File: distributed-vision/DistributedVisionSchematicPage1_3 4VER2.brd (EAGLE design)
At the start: 123 x 98.5 mm, 157 parts, among them J1 USBR-A-D-F-O-TH, J12 ARJM11C7-104-AB-EW2, J2 RASPBERRRY_COMPUTE_CM3, J6 DM3D-SF, J8 1-84952-5, J9 1-84952-5, Q2 BSS127, Q3 BSS127, Q7 25 MHz, U1 LM26420XMH, U11 IFX91041, U12 TPS26600PWPR, U3 LAN9513-JZXQFN64_9X9MC_MCH-M, U8 SP3003-02, U9 SP3003-02, X1 JST-XH-02-PIN-LONG-PAD

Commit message: Version 3
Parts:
- removed D6: GREEN, RoboJackets-LEDs:LED-0603
- removed JP1: (no value), RoboJackets-Connectors:1X02
- removed Q2, Q3: BSS127, RoboJackets-Discrete:SOT-23-3
- removed R1: 47k, rcl:R0603
- removed R4: 100k, rcl:R0603
- removed R44: 470r, rcl:R0603
- moved H1 81.0 mm to (101.9, 86.1)
- moved C18 21.5 mm to (106.0, 32.8)
- moved L7 19.8 mm to (12.4, 15.1), turned to 180 degrees
- moved R8 17.1 mm to (16.1, 22.0)
- moved C86 16.1 mm to (20.2, 33.9)
- moved C81 15.8 mm to (104.8, 18.0)
- moved C35 14.9 mm to (108.1, 37.9)
- moved C80 14.8 mm to (106.9, 20.6)
- moved C82 14.3 mm to (107.8, 30.3)
- moved U9 14.3 mm to (15.9, 18.2)
- moved H2 14.1 mm to (22.3, 86.1)
- moved C6 13.4 mm to (107.7, 24.1)
- moved C24 13.4 mm to (10.2, 26.9)
- moved C62 13.4 mm to (9.97, 38.9)
- moved C78 13.4 mm to (107.8, 27.3)
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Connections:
- removed net AGND: H1.B2,8, H2.B2,8
- removed net EMMC_DISABLE_N: J2.2, Q2.3
- removed net EMMC_EN_N_1V8: J2.90, Q3.1, R4.1
- removed net N$31: Q2.2, Q3.3, R44.1
- removed net N$32: D6.C, R44.2
- removed net N$33: JP1.2, Q2.1, R1.2
- net +1.8V: no longer R4.2
- net +3.3V: no longer D6.A
- net +5V: no longer JP1.1
- net GND: no longer Q3.2, R1.1
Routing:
- net EMMC_EN_N_1V8: track 85.1 -> 0.00 mm, vias 3 -> 0
- net G_LED+: track 6.71 -> 60.6 mm, vias 0 -> 4
- net N$56: track 43.1 -> 93.7 mm
- net GND: track 1089.3 -> 1047.8 mm, vias 66 -> 67
- net +3.3V-A: track 84.0 -> 111.5 mm
- net EMMC_DISABLE_N: track 22.8 -> 0.00 mm
- net TVCC: track 59.1 -> 37.1 mm, vias 3 -> 1
- net USBDP3: track 74.3 -> 52.7 mm, vias 3 -> 2
- net N$33: track 18.8 -> 0.00 mm, vias 2 -> 0
- net N$40: track 75.0 -> 57.4 mm
- net N$25: track 11.7 -> 29.2 mm
- net USBDM2: track 72.9 -> 57.0 mm
- net N$31: track 15.6 -> 0.00 mm, vias 2 -> 0
- net +3.3V: track 579.1 -> 594.3 mm, vias 36 -> 39
- net VBATT: track 37.5 -> 51.7 mm, vias 3 -> 4
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- added copper zone on layer 1, net GND
- added copper zone on layer 16, net GND
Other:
- board size 123 x 98.5 mm -> 104 x 97.5 mm

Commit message: Joe Cleanup Schematic
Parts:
- removed C53: 100n, rcl:C0402
- removed R2: (no value), rcl:R0603
- removed R31: 4.7k, RoboJackets-Resistors:RC0805N
- F2: value 1A (Trip) -> 2A; device ethernet_poe:0ZCG_BEL -> RoboJackets-Fuses:1812
- R26: value 12k -> 12k, 1.0%
- R27: value 12.4k -> 12.4k, 1.0%
- R7: value 5r1 -> 5.1
- moved C75 117.6 mm to (8.00, -14.0)
- moved R14 94.2 mm to (8.00, -37.0)
- moved R7 89.3 mm to (8.00, -42.0), turned to 0 degrees
- moved F2 81.0 mm to (10.0, -49.0), turned to 0 degrees
- moved R13 77.1 mm to (18.0, -32.0), turned to 0 degrees
- moved R9 77.1 mm to (18.0, -37.0)
- moved C25 62.7 mm to (15.0, -24.0), turned to 0 degrees
- moved R8 59.1 mm to (13.0, -37.0), flipped to the top, turned to 0 degrees
- moved C24 59.0 mm to (13.0, -32.0)
- moved F1 58.1 mm to (10.0, -26.0), turned to 0 degrees
- moved C86 54.3 mm to (8.00, -19.0), turned to 0 degrees
- moved C23 52.3 mm to (8.00, -32.0)
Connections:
- removed net BD+: J1.A03, U9.4
- removed net N$61: C53.1, R31.1, U3.12
- removed net USBDM3: U3.3
- removed net USBDP2: U3.2
- removed net USBDP3: J1.B02, J1.B03, U3.4, U8.4, U8.6
- removed net USB_DM: U3.58
- removed net USB_DP: U3.59
- removed net USB_OTGID: J2.168, R2.2
- removed net VBATT: C18.1, C19.1, C21.1, C22.1, C35.1, J2.197, J2.198, J2.199, J2.200
- new net N$12: U8.6
- new net N$3: R13.2, U1.8
- new net N$6: U9.4
- new net N$7: U8.4
- new net RX_P1: R9.2, U1.12
- new net USB0_N: J2.167, U3.58
- new net USB0_P: J2.165, U3.59
- new net USB2_N: J1.A02, U3.1
- new net USB2_P: J1.A03, U3.2
- new net USB3_N: J1.B02, U3.3
- new net USB3_P: J1.B03, U3.4
- net +3.3V: now also U3.12; no longer R31.2
- net +5V: now also C18.1, C19.1, C21.1, C22.1, C35.1, J2.197, J2.198, J2.199, J2.200
- net BVCC: no longer J1.A01
- net GND: now also J1.S1, J1.S2, J1.S3, J1.S4, J2.168; no longer C53.2, R2.1
- net RX_P: no longer R9.2, U1.12
- net TVCC: now also J1.A01
- net USBDM2: no longer J1.A02, U3.1
- net VDD18CORE: no longer R13.2, U1.8
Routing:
- net +5V: track 172.0 -> 89.1 mm, vias 17 -> 9
- net N$40: track 57.4 -> 0.00 mm, vias 3 -> 0
- net USBDP3: track 52.7 -> 0.00 mm, vias 2 -> 0
- net VBATT: track 51.7 -> 0.00 mm, vias 4 -> 0
- net USBDM2: track 57.0 -> 5.68 mm, vias 3 -> 1
- net USB2_N: track 0.00 -> 49.1 mm, vias 0 -> 2
- net GND: track 1047.8 -> 1001.1 mm, vias 67 -> 65
- net N$5: track 39.7 -> 0.00 mm, vias 4 -> 0
- net +3.3V: track 594.3 -> 561.5 mm, vias 39 -> 42
- net USB_OTGID: track 20.0 -> 0.00 mm
- net USB3_P: track 0.00 -> 13.4 mm, vias 0 -> 2
- net TVCC: track 37.1 -> 24.4 mm
- net +5V_PREFUSE: track 54.1 -> 42.6 mm
- net N$61: track 11.3 -> 0.00 mm, vias 3 -> 0
- net BVCC: track 56.5 -> 48.1 mm
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
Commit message: Joe Small board cleanup
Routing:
- net GND: track 1001.1 -> 8.45 mm, vias 65 -> 3
- net +3.3V-A: track 111.5 -> 106.8 mm
- net VDD18CORE: track 113.7 -> 112.6 mm

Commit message: Updated Values in DisbVision sch
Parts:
- C10, C15, C16, C21, C42, C45, C46, C5, C50, C6, C60, C63, C68, C69, C70, C71, C78, C81, C82, C83, C84, C88, C91: value 100n -> 100nF
- C102, C103, C12, C17, C22, C35, C7, C73: value 10u -> 10uF
- C13, C18, C19, C20, C33, C4, C51, C52, C58, C61, C75, C76, C77, C8, C80, C85, C86, C9: value 10n -> 10nF
- C14, C64: value 1u -> 1uF
- C23, C24, C26, C27, C28, C29: value 22u -> 22uF
- C25: value 470n -> 470nF
- C43, C44, C62: value 4u7 -> 4.7uF
- C65, C66: value 33p -> 33pF

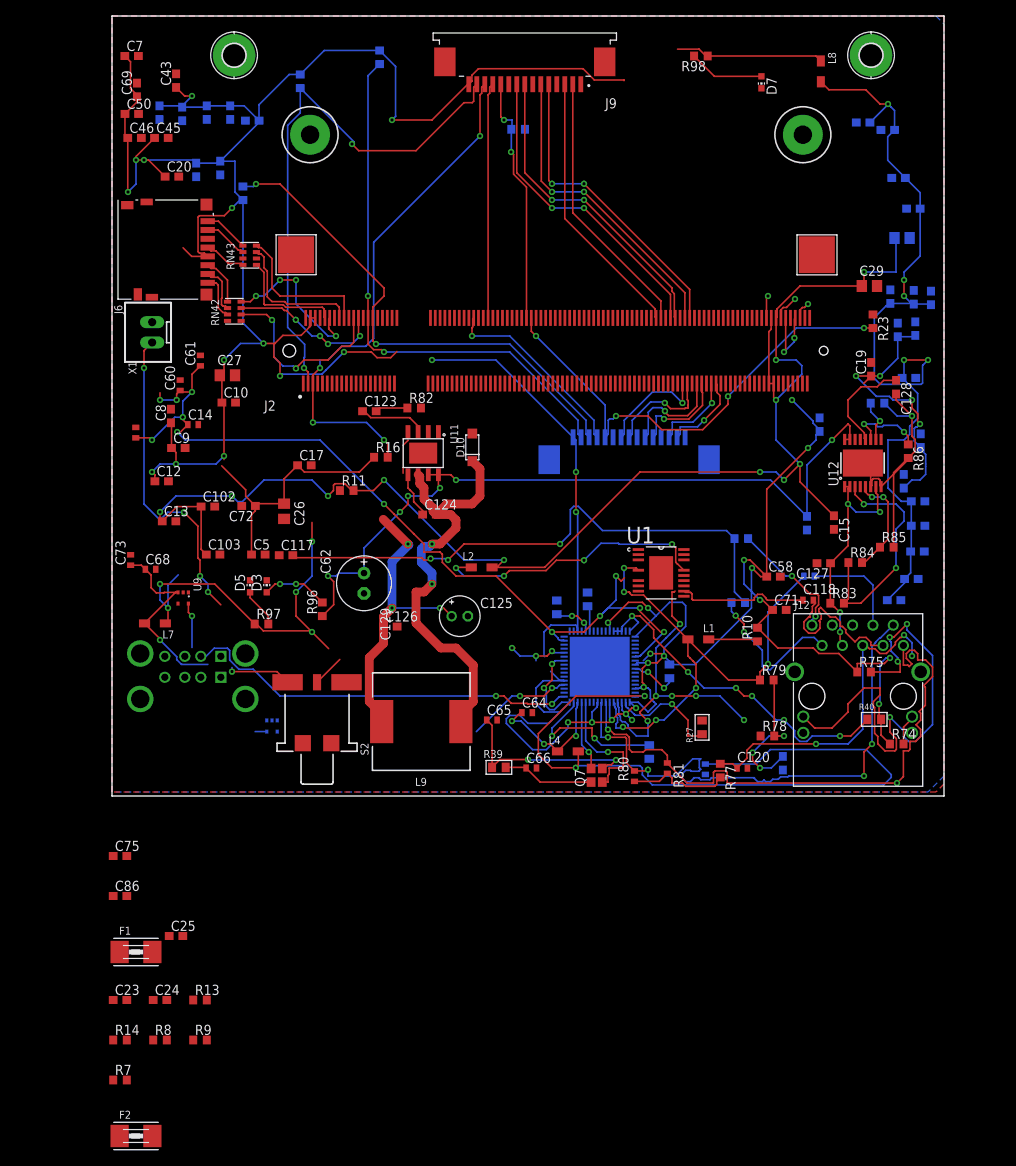
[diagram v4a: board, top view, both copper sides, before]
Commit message: Routed Board Based off Schematic Changes
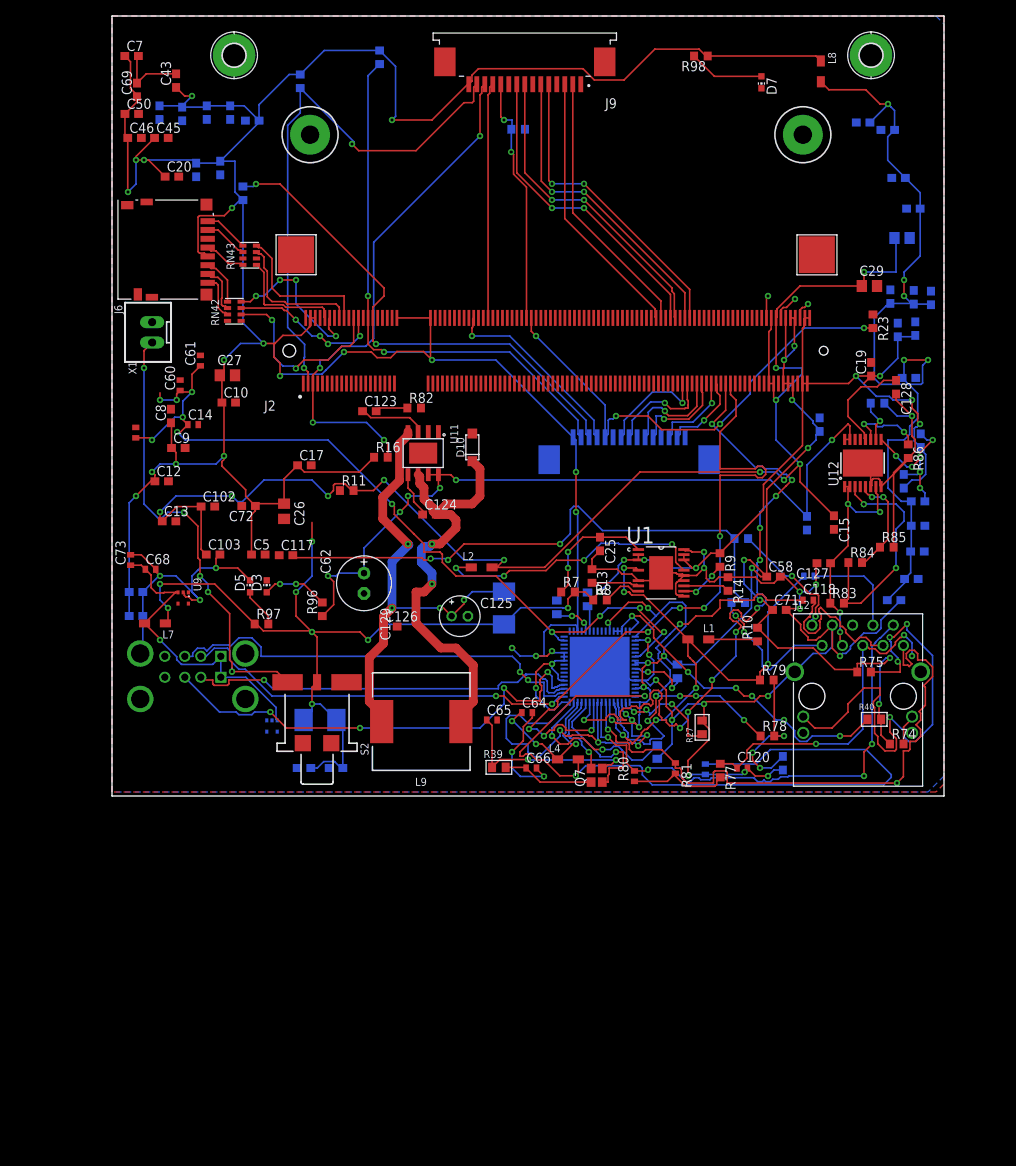
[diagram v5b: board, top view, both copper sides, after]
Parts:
- C72, C79: value 100n -> 100nF
- R7: value 5.1 -> 5.1k
- moved R14 95.0 mm to (84.0, 20.0), turned to 270 degrees
- moved R9 88.5 mm to (83.0, 23.0), turned to 270 degrees
- moved R7 82.8 mm to (64.0, 19.0)
- moved F2 80.4 mm to (56.0, 17.0), flipped to the bottom, turned to 270 degrees
- moved R8 77.8 mm to (68.0, 18.0)
- moved C25 72.2 mm to (68.0, 25.0), turned to 270 degrees
- moved R13 72.2 mm to (67.0, 21.0), turned to 270 degrees
- moved C23 39.6 mm to (35.0, -3.00), flipped to the bottom
- moved F1 37.0 mm to (33.0, 3.00), flipped to the bottom
- moved C86 35.1 mm to (10.0, 16.0), flipped to the bottom, turned to 180 degrees
- moved C24 34.1 mm to (31.0, -3.00), flipped to the bottom
- moved C75 33.1 mm to (10.0, 19.0), flipped to the bottom, turned to 180 degrees
- moved R26 1.00 mm to (75.2, -1.00)
- moved R28 1.00 mm to (77.7, 9.08)
- moved R81 1.00 mm to (77.4, -3.02)
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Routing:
- net GND: track 8.45 -> 242.8 mm, vias 3 -> 29
- net +5V: track 89.1 -> 208.0 mm, vias 9 -> 16
- net USB0_P: track 0.00 -> 87.1 mm, vias 0 -> 11
- net USB0_N: track 0.00 -> 83.5 mm, vias 0 -> 7
- net USB2_P: track 0.00 -> 54.5 mm, vias 0 -> 2
- net +3.3V: track 561.5 -> 615.5 mm, vias 42 -> 44
- net USB3_N: track 0.00 -> 50.2 mm, vias 0 -> 1
- net USB3_P: track 13.4 -> 59.3 mm, vias 2 -> 4
- net N$5: track 0.00 -> 15.6 mm, vias 0 -> 2
- net +5V_PREFUSE: track 42.6 -> 57.6 mm, vias 3 -> 4
- net TVCC: track 24.4 -> 39.2 mm
- net BVCC: track 48.1 -> 57.0 mm
- net TX_N: track 71.4 -> 62.8 mm
- net VDD18CORE: track 112.6 -> 105.9 mm, vias 12 -> 11
- net N$3: track 0.00 -> 5.95 mm
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
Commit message: Updated Gerber
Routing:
- net +5V: track 208.0 -> 213.3 mm
- net GND: track 242.8 -> 246.9 mm
- net USB2_P: track 54.5 -> 56.3 mm
- net RX_FILTER: track 18.8 -> 17.4 mm
- net N$56: track 98.1 -> 96.9 mm
- net USB0_P: track 87.1 -> 88.0 mm

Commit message: BOM/PnP Changes
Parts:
- R40: value 4k7 -> 4.7k
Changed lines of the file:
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@@
 <drawing>
 <settings>
-<setting alwaysvectorfont="yes"/>
+<setting alwaysvectorfont="no"/>
 <setting verticaltext="up"/>
 </settings>
@@
 <attribute name="VALUE" x="53.36" y="-4.92" size="0.8" layer="27"/>
 </element>
-<element name="R40" library="RoboJackets-Resistors" package="RC0805N" value="4k7" x="102.28" y="3.08" smashed="yes">
+<element name="R40" library="RoboJackets-Resistors" package="RC0805N" value="4.7k" x="102.28" y="3.08" smashed="yes">
 <attribute name="DKPN" value="P50LLCT-ND  " x="148" y="-129" size="1.778" layer="27" display="off"/>
 <attribute name="NAME" x="100.3464" y="4.25" size="0.8" layer="25" rot="SR0"/>
